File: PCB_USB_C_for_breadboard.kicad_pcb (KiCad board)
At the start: 2 copper layers, 22.9 x 17.8 mm, 13 parts, among them J1 USB_C_Receptacle_USB2.0_16P, J2 Conn_01x02_Pin, J3 Conn_01x02_Pin, J4 Conn_01x03_Pin, J5 Conn_01x05_Socket, SW1 SW_SPDT, U1 NJM2845DL1-33

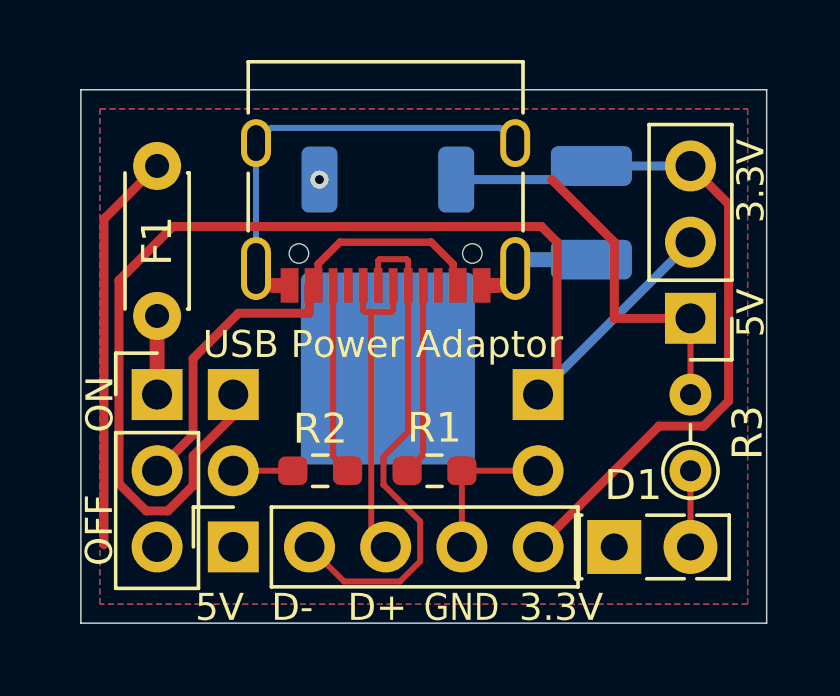
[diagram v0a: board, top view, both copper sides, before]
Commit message: Rev. 2
* 基板サイズを拡大
* SW1の位置を調整
* SMDのポリヒューズを取り付け可能に
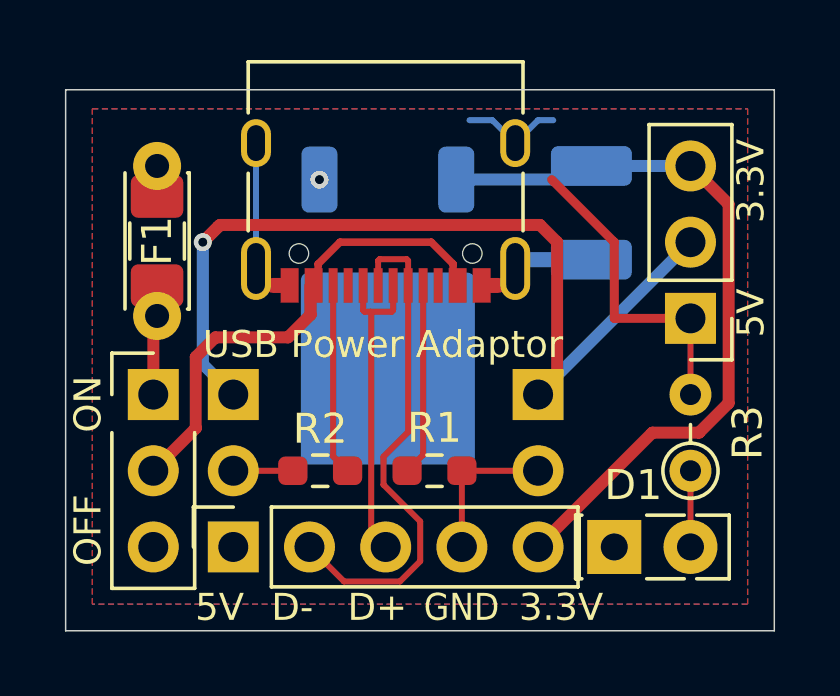
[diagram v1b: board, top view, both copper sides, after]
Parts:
- added F2: Polyfuse_Small, Fuse:Fuse_1206_3216Metric_Pad1.42x1.75mm_HandSolder, F.Cu at (91.4, 33.0)
- moved SW1 0.13 mm to (91.3, 38.1)
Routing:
- net +5V: track 24.6 -> 10.6 mm
- net /VDD: track 41.7 -> 31.1 mm, vias 0 -> 1
- net GND: track 28.2 -> 22.5 mm
- net Net-(SW1-B): track 16.2 -> 17.2 mm
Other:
- board size 22.9 x 17.8 mm -> 23.6 x 18 mm

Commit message: Rev. 3
* U1をNJM2845DL1-33からLM1117GS-3.3に変更
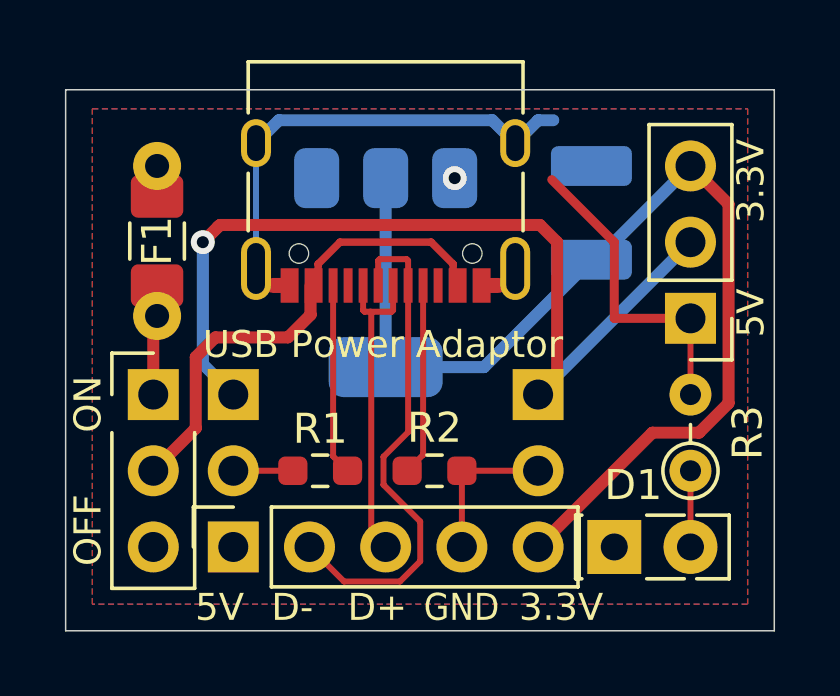
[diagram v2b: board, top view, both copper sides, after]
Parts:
- U1: value NJM2845DL1-33 -> LM1117GS-3.3; footprint Package_TO_SOT_SMD:TO-252-2 -> Package_TO_SOT_SMD:SOT-223-3_TabPin2
- moved U1 1.94 mm to (99.1, 34.0)
- turned C1 to 90 degrees
- renumbered R2 to R1, R1 to R2
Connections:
- U1 pad 1: +5V -> GND
- U1 pad 2: GND -> +3.3V
- U1 pad 3: +3.3V -> +5V
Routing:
- net +3.3V: track 24.8 -> 38.8 mm
- net GND: track 22.5 -> 25.6 mm

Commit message: 微調整
R3を上下反転。
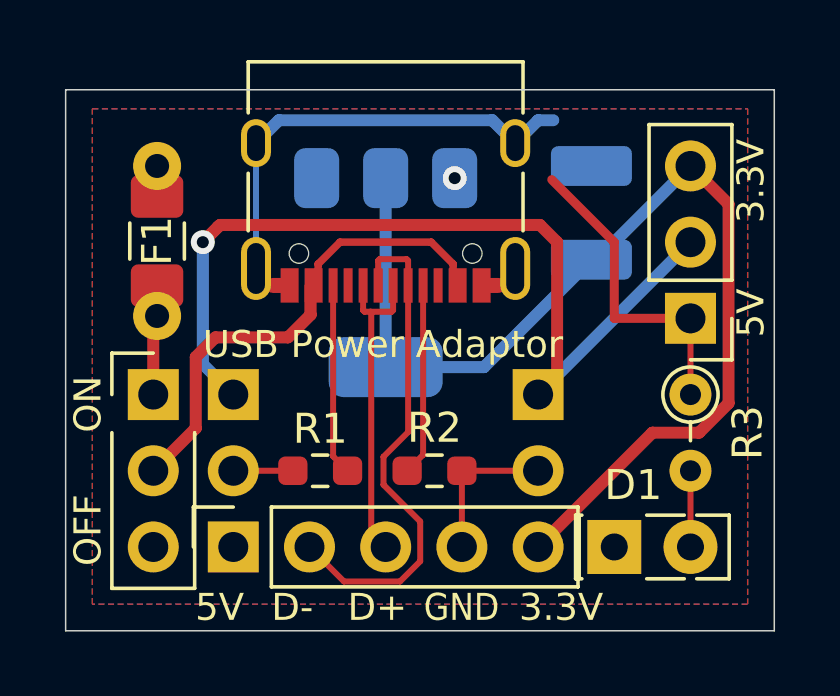
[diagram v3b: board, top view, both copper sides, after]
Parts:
- moved R3 2.54 mm to (109.2, 38.1), turned to -90 degrees
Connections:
- R3 pad 1: Net-(D1-A) -> +5V
- R3 pad 2: +5V -> Net-(D1-A)
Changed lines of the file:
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@@
 	(title_block
 		(title "USB Type-C Power Adaptor for Breadboard")
-		(date "2025-07-14")
+		(date "2025-08-02")
 		(rev "3")
 		(company "K.Takata")
@@
 			)
 		)
-		(property "Datasheet" ""
+		(property "Datasheet" "~"
 			(at 0 0 90)
 			(layer "F.Fab")
@@
 	(footprint "Resistor_THT:R_Axial_DIN0204_L3.6mm_D1.6mm_P2.54mm_Vertical"
 		(layer "F.Cu")
-		(at 109.22 40.64 90)
+		(at 109.22 38.1 -90)
 		(descr "Resistor, Axial_DIN0204 series, Axial, Vertical, pin pitch=2.54mm, 0.167W, length*diameter=3.6*1.6mm^2, http://cdn-reichelt.de/documents/datenblatt/B400/1_4W%23YAG.pdf")
 		(tags "Resistor Axial_DIN0204 series Axial Vertical pin pitch 2.54mm 0.167W length 3.6mm diameter 1.6mm")
 		(property "Reference" "R3"
-			(at 1.27 1.905 90)
+			(at 1.27 -1.905 90)
 			(layer "F.SilkS")
 			(effects
@@
 			)
 		)
-		(property "Datasheet" ""
+		(property "Datasheet" "~"
 			(at 0 0 90)
 			(layer "F.Fab")
@@
 		)
 		(pad "1" thru_hole circle
-			(at 0 0 90)
+			(at 0 0 270)
+			(size 1.4 1.4)
+			(drill 0.7)
+			(layers "*.Cu" "*.Mask")
+			(remove_unused_layers no)
+			(net 4 "+5V")
+			(pintype "passive")
+		)
+		(pad "2" thru_hole circle
+			(at 2.54 0 270)
 			(size 1.4 1.4)
 			(drill 0.7)
@@
 			(remove_unused_layers no)
 			(net 3 "Net-(D1-A)")
-			(pintype "passive")
-		)
-		(pad "2" thru_hole circle
-			(at 2.54 0 90)
-			(size 1.4 1.4)
-			(drill 0.7)
-			(layers "*.Cu" "*.Mask")
-			(remove_unused_layers no)
-			(net 4 "+5V")
 			(pintype "passive")
 		)
@@
 			)
 		)
-		(property "Datasheet" ""
+		(property "Datasheet" "~"
 			(at 0 0 0)
 			(layer "F.Fab")
@@
 			)
 		)
-		(property "Datasheet" ""
+		(property "Datasheet" "~"
 			(at 0 0 0)
 			(layer "F.Fab")
@@
 			)
 		)
-		(property "Datasheet" ""
+		(property "Datasheet" "~"
 			(at 0 0 90)
 			(layer "F.Fab")
@@
 			)
 		)
-		(property "Datasheet" ""
+		(property "Datasheet" "~"
 			(at 0 0 0)
 			(layer "F.Fab")
@@
 			)
 		)
-		(property "Datasheet" ""
+		(property "Datasheet" "~"
 			(at 0 0 0)
 			(layer "F.Fab")
@@
 			)
 		)
-		(property "Datasheet" ""
+		(property "Datasheet" "~"
 			(at 0 0 0)
 			(layer "F.Fab")
@@
 			)
 		)
-		(property "Datasheet" ""
+		(property "Datasheet" "~"
 			(at 0 0 90)
 			(layer "F.Fab")
@@
 			)
 		)
-		(property "Datasheet" ""
+		(property "Datasheet" "~"
 			(at 0 0 0)
 			(layer "B.Fab")
@@
 			)
 		)
-		(property "Datasheet" ""
+		(property "Datasheet" "~"
 			(at 0 0 90)
 			(layer "B.Fab")
@@
 			)
 		)
-		(property "Datasheet" ""
+		(property "Datasheet" "~"
 			(at 0 0 0)
 			(layer "B.Fab")

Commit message: Adjust SW1 position
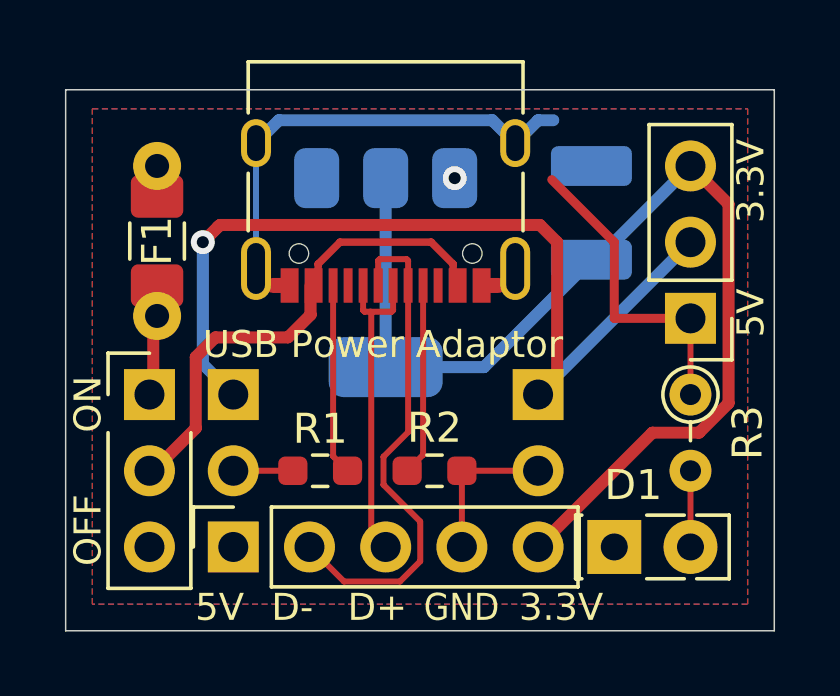
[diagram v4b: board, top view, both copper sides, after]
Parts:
- moved SW1 0.13 mm to (91.2, 38.1)
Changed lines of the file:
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@@
 	(footprint "Connector_PinHeader_2.54mm:PinHeader_1x03_P2.54mm_Vertical"
 		(layer "F.Cu")
-		(at 91.313 38.1)
+		(at 91.186 38.1)
 		(descr "Through hole straight pin header, 1x03, 2.54mm pitch, single row")
 		(tags "Through hole pin header THT 1x03 2.54mm single row")
